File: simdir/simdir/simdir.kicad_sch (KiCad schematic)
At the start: 5 parts, among them U2 MASWSS0178, U3 MASWSS0178, U4 MASWSS0178, U5 MASWSS0178, U6 MASWSS0178

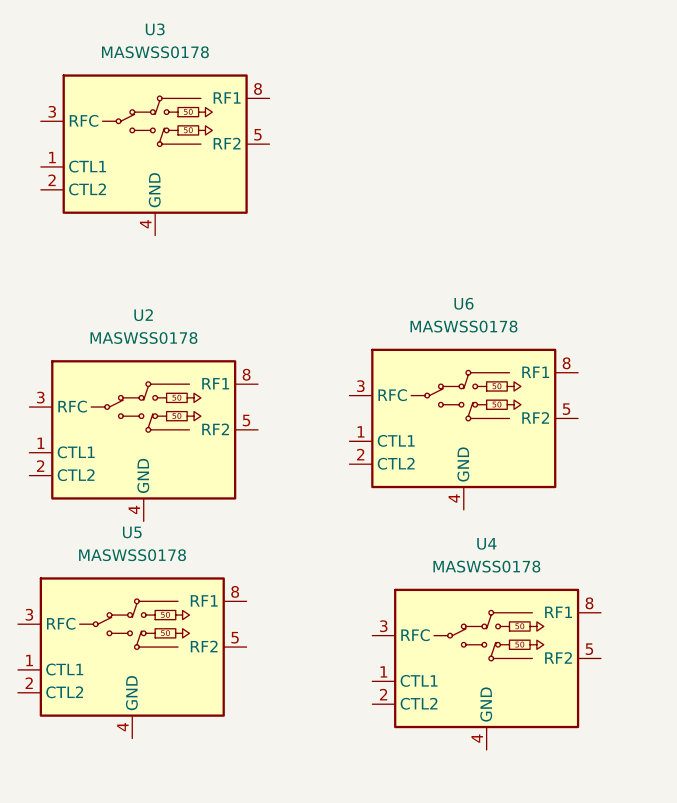
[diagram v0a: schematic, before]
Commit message: Added channel block.
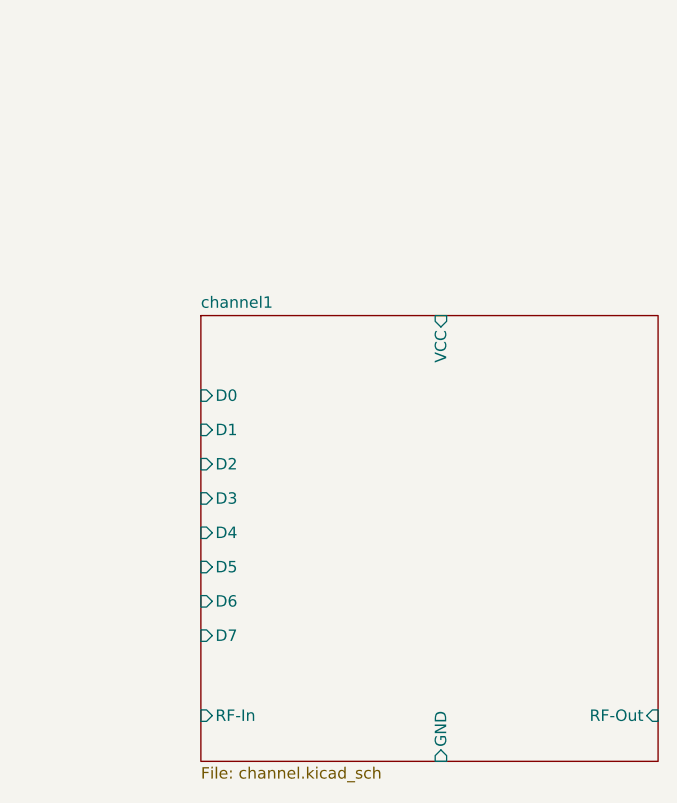
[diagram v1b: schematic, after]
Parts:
- removed U2, U3, U4, U5, U6: MASWSS0178, hand:MSOP-8-1EP_3x3mm_P0.65mm_EP1.73x1.85mm_hand, symbol hand:MASWSS0178
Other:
- added sheet channel1 (channel.kicad_sch)

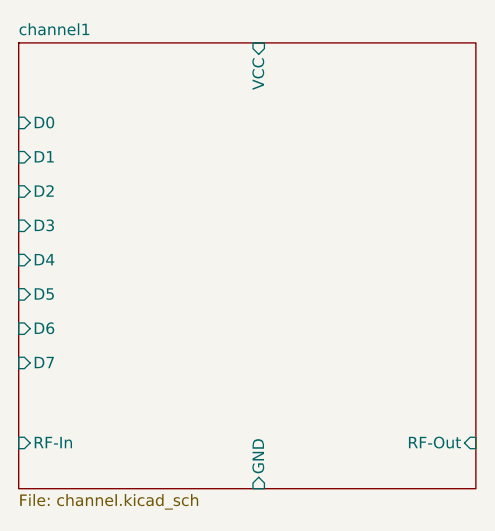
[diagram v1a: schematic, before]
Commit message: Fixed minor issues with channel pins.
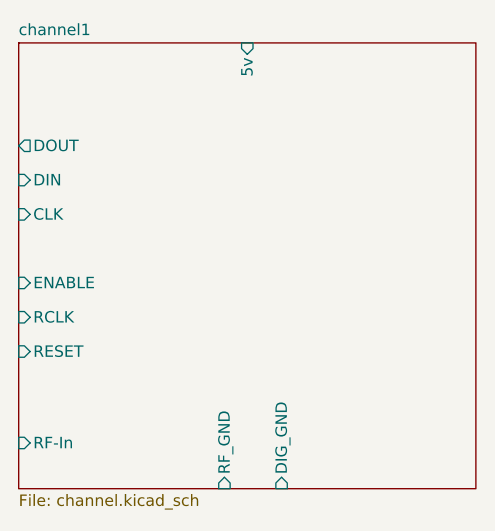
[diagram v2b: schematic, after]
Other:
- sheet channel1 ports: added 5v, CLK, DIG_GND, DIN, DOUT, ENABLE, RCLK, RESET, RF_GND; removed D0, D1, D2, D3, D4, D5, D6, D7, GND, RF-Out, VCC
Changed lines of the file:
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@@
-			)
-		)
-		(pin "D0" input
-			(at 44.45 96.52 180)
-			(effects
-				(font
-					(size 1.27 1.27)
-				)
-				(justify left)
-			)
-		)
-		(pin "D1" input
-			(at 44.45 100.33 180)
-			(effects
-				(font
-					(size 1.27 1.27)
-				)
-				(justify left)
-			)
-		)
-		(pin "D2" input
-			(at 44.45 104.14 180)
-			(effects
-				(font
-					(size 1.27 1.27)
-				)
-				(justify left)
-			)
-		)
-		(pin "D3" input
-			(at 44.45 107.95 180)
-			(effects
-				(font
-					(size 1.27 1.27)
-				)
-				(justify left)
-			)
-		)
-		(pin "D4" input
-			(at 44.45 111.76 180)
-			(effects
-				(font
-					(size 1.27 1.27)
-				)
-				(justify left)
-			)
-		)
-		(pin "D5" input
-			(at 44.45 115.57 180)
-			(effects
-				(font
-					(size 1.27 1.27)
-				)
-				(justify left)
-			)
-		)
-		(pin "D6" input
-			(at 44.45 119.38 180)
-			(effects
-				(font
-					(size 1.27 1.27)
-				)
-				(justify left)
-			)
-		)
-		(pin "D7" input
-			(at 44.45 123.19 180)
-			(effects
-				(font
-					(size 1.27 1.27)
-				)
-				(justify left)
-			)
-		)
-		(pin "GND" input
-			(at 71.12 137.16 270)
-			(effects
-				(font
-					(size 1.27 1.27)
-				)
-				(justify left)
 			)
 		)
@@
 			)
 		)
-		(pin "RF-Out" input
-			(at 95.25 132.08 0)
+		(pin "5v" input
+			(at 69.85 87.63 90)
 			(effects
 				(font
@@
 			)
 		)
-		(pin "VCC" input
-			(at 71.12 87.63 90)
+		(pin "CLK" input
+			(at 44.45 106.68 180)
 			(effects
 				(font
 					(size 1.27 1.27)
 				)
-				(justify right)
+				(justify left)
 			)
 		)
+		(pin "DIG_GND" input
+			(at 73.66 137.16 270)
+			(effects
+				(font
+					(size 1.27 1.27)
+				)
+				(justify left)
+			)
+		)
+		(pin "DIN" input
+			(at 44.45 102.87 180)
+			(effects
+				(font
+					(size 1.27 1.27)
+				)
+				(justify left)
+			)
+		)
+		(pin "DOUT" output
+			(at 44.45 99.06 180)
+			(effects
+				(font
+					(size 1.27 1.27)
+				)
+				(justify left)
+			)
+		)
+		(pin "ENABLE" input
+			(at 44.45 114.3 180)
+			(effects
+				(font
+					(size 1.27 1.27)
+				)
+				(justify left)
+			)
+		)
+		(pin "RCLK" input
+			(at 44.45 118.11 180)
+			(effects
+				(font
+					(size 1.27 1.27)
+				)
+				(justify left)
+			)
+		)
+		(pin "RESET" input
+			(at 44.45 121.92 180)
+			(effects
+				(font
+					(size 1.27 1.27)
+				)
+				(justify left)
+			)
+		)
+		(pin "RF_GND" input
+			(at 67.31 137.16 270)
+			(effects
+				(font
+					(size 1.27 1.27)
+				)
+				(justify left)
+			)
+		)

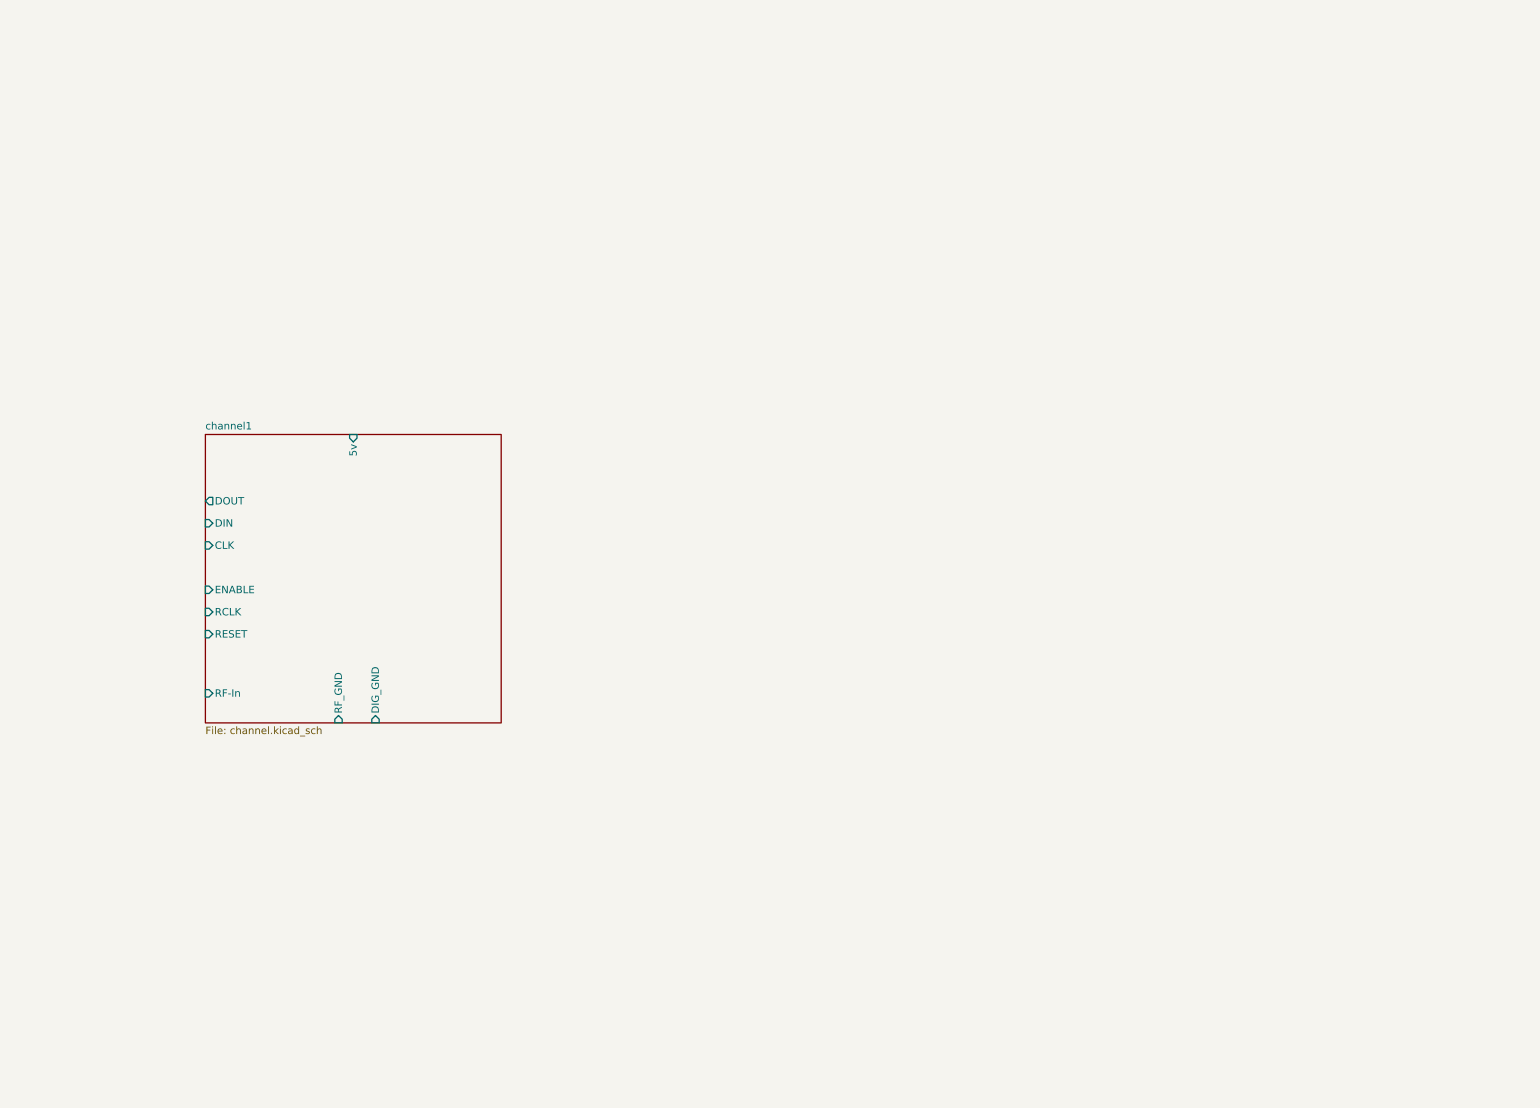
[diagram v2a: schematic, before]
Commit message: Duplicated the channels.
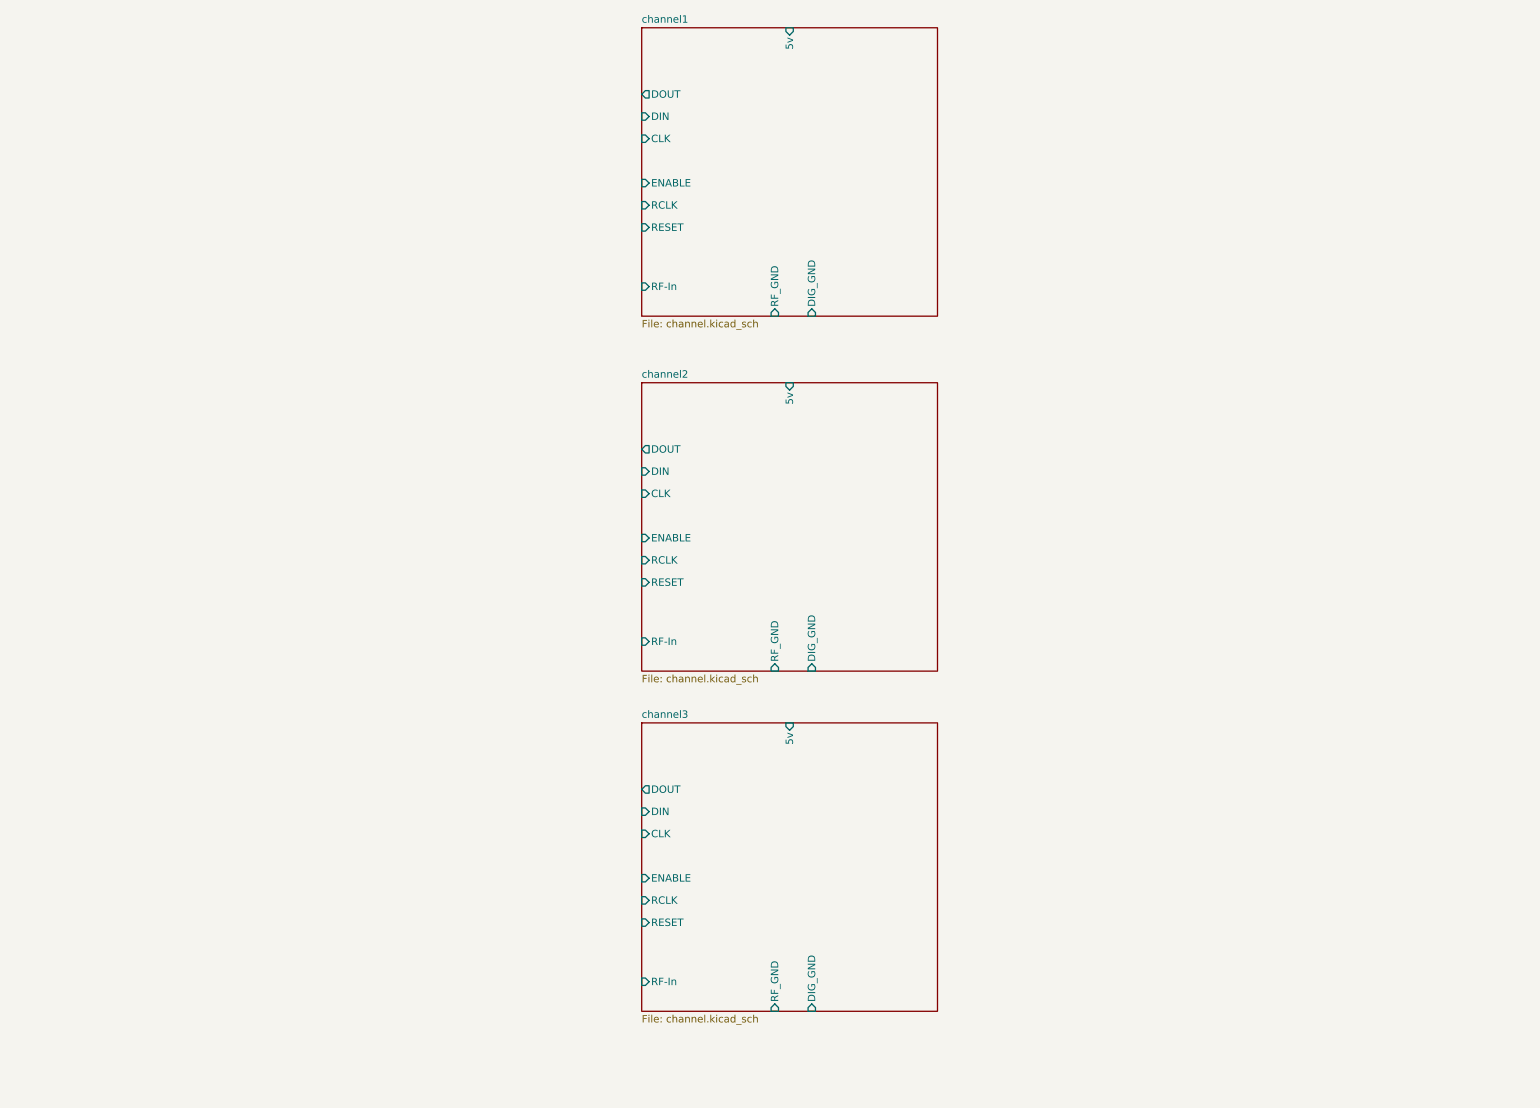
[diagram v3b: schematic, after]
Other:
- added sheet channel2 (channel.kicad_sch)
- added sheet channel3 (channel.kicad_sch)

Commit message: Fixed layout issues & added splitter.
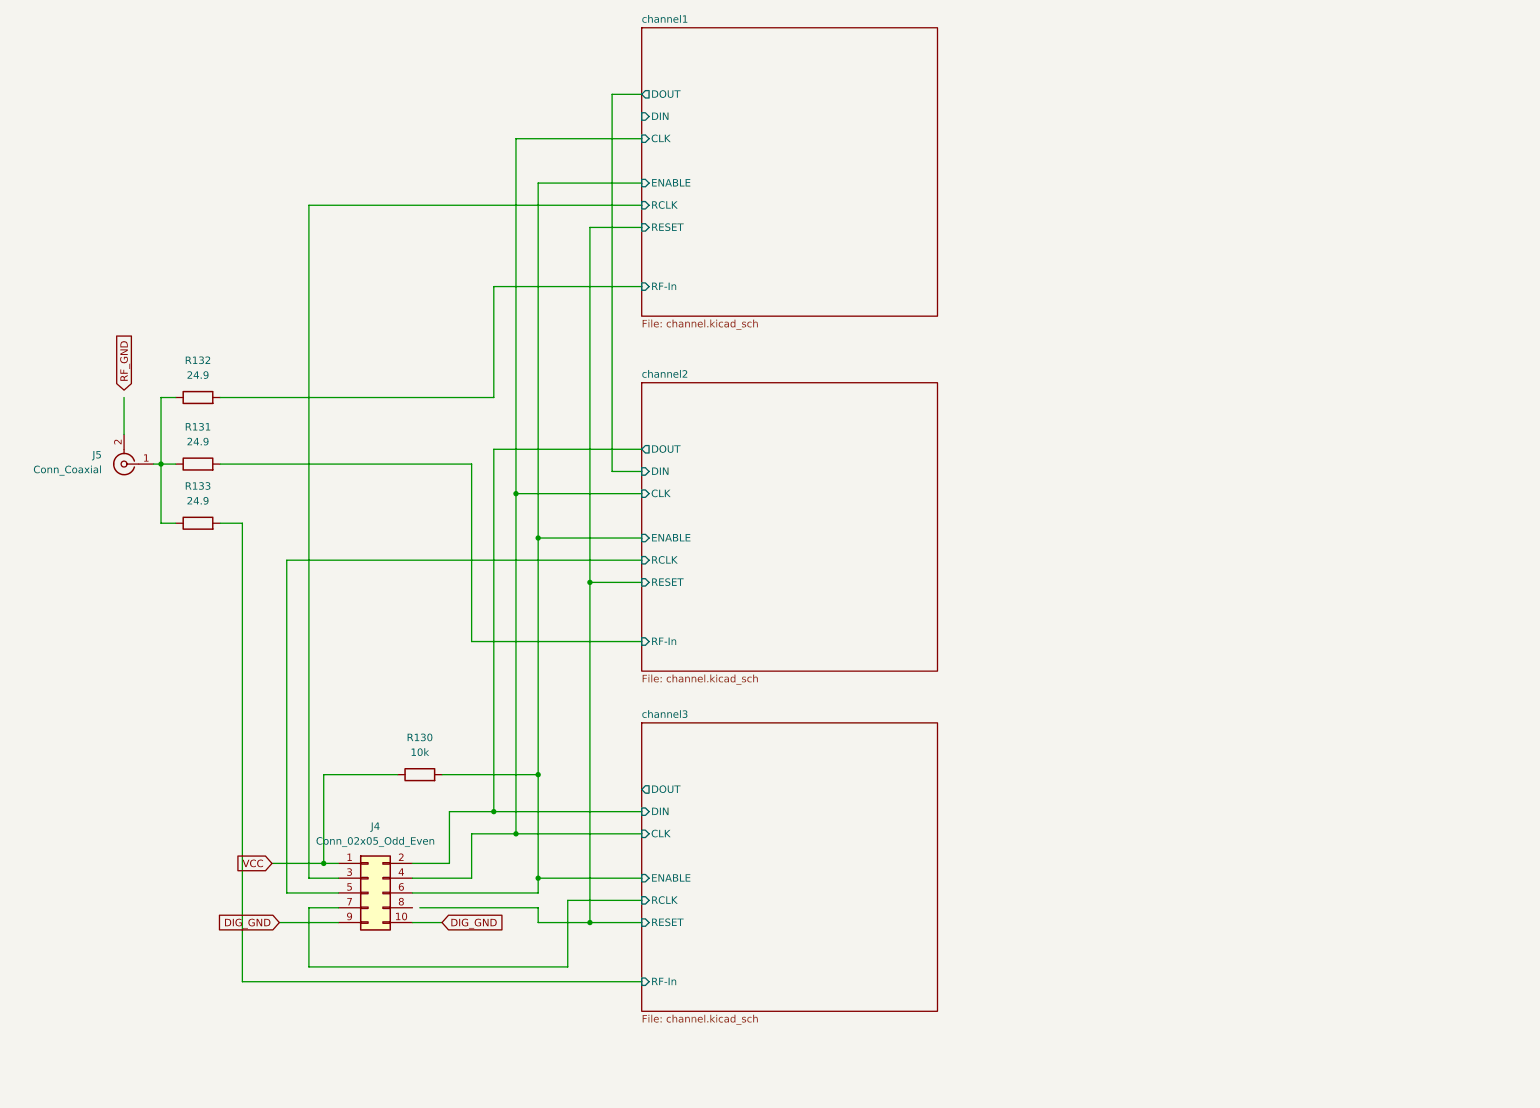
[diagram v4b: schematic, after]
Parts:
- added J4: Conn_02x05_Odd_Even, Connector_PinHeader_2.54mm:PinHeader_2x05_P2.54mm_Vertical, symbol Connector_Generic:Conn_02x05_Odd_Even
- added J5: Conn_Coaxial, Connector_Coaxial:SMA_Amphenol_132289_EdgeMount, symbol Connector:Conn_Coaxial
- added R130: 10k, Resistor_SMD:R_0805_2012Metric_Pad1.20x1.40mm_HandSolder, symbol Device:R
- added R131, R132, R133: 24.9, Resistor_SMD:R_0805_2012Metric_Pad1.20x1.40mm_HandSolder, symbol Device:R
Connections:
- net channel1/CLK: now also J4.4 (Pin_4)
- net channel1/ENABLE: now also J4.6 (Pin_6), R130.2
- net channel1/RCLK: now also J4.3 (Pin_3)
- net channel1/RF-In: now also R132.2
- net channel2/DOUT: now also J4.2 (Pin_2)
- net channel2/RCLK: now also J4.5 (Pin_5)
- net channel2/RF-In: now also R131.2
- net channel3/RCLK: now also J4.7 (Pin_7)
- net channel3/RF-In: now also R133.2
- new net: J5.1 (In), R131.1, R132.1, R133.1
- new net DIG_GND: J4.10 (Pin_10), J4.9 (Pin_9)
- new net VCC: J4.1 (Pin_1), R130.1
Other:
- sheet channel1 ports: added none; removed 5v, DIG_GND, RF_GND
- sheet channel2 ports: added none; removed 5v, DIG_GND, RF_GND
- sheet channel3 ports: added none; removed 5v, DIG_GND, RF_GND

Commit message: Finalized simulation PCB.
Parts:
- added C7: 470n, Capacitor_THT:C_Radial_D10.0mm_H12.5mm_P5.00mm, symbol Device:C
- added C8: 22uF, Capacitor_THT:CP_Radial_D6.3mm_P2.50mm, symbol Device:C_Polarized
- added FB4: FerriteBead, Inductor_SMD:L_0805_2012Metric_Pad1.05x1.20mm_HandSolder, symbol Device:FerriteBead
- added J6: Conn_01x02, Connector_PinHeader_2.54mm:PinHeader_1x02_P2.54mm_Vertical, symbol Connector_Generic:Conn_01x02
- added U58: LM2940CT-5.0, Package_TO_SOT_THT:TO-220-3_Vertical, symbol Regulator_Linear:LM78M05_TO220
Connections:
- net DIG_GND: now also C7.2, C8.2, FB4.2, J6.2 (Pin_2), U58.2 (GND)
- net RF_GND: now also J5.2 (Ext), FB4.1
- net channel1/DIN: now also J4.2 (Pin_2)
- net channel1/RESET: now also J4.8 (Pin_8)
- net channel2/DOUT: no longer J4.2 (Pin_2)
- net VCC renamed 5v
- net 5v: now also C8.1, U58.3 (VO)
- new net: C7.1, J6.1 (Pin_1), U58.1 (VI)

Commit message: Added gerber files.
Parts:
- added R134: 24.9, Resistor_SMD:R_0805_2012Metric_Pad1.20x1.40mm_HandSolder, symbol Device:R
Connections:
- net at R131.1, R132.1, R133.1: now also R134.2; no longer J5.1 (In)
- new net: J5.1 (In), R134.1
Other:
- moved on the sheet: C7, C8, FB4, J4, J6, R130, R131, R132, R133, U58

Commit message: Fixed PCB layout.
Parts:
- removed FB4: FerriteBead, Inductor_SMD:L_0805_2012Metric_Pad1.05x1.20mm_HandSolder, symbol Device:FerriteBead
- added H1, H2, H3, H4: MountingHole_Pad, MountingHole:MountingHole_4.3mm_M4_Pad_Via, symbol Mechanical:MountingHole_Pad
- added NT1: NetTie_2, NetTie:NetTie-2_THT_Pad1.0mm, symbol Device:NetTie_2
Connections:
- net DIG_GND: now also H1.1, H2.1, NT1.1
- net RF_GND: now also H3.1, H4.1, NT1.2

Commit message: Use smaller capacitor and tab-down regulator.
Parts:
- C7: footprint Capacitor_THT:C_Radial_D10.0mm_H12.5mm_P5.00mm -> Capacitor_THT:C_Disc_D4.3mm_W1.9mm_P5.00mm
- U58: footprint Package_TO_SOT_THT:TO-220-3_Vertical -> Package_TO_SOT_THT:TO-220-3_Horizontal_TabDown
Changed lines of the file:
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@@
 			)
 		)
-		(property "Footprint" "Capacitor_THT:C_Radial_D10.0mm_H12.5mm_P5.00mm"
+		(property "Footprint" "Capacitor_THT:C_Disc_D4.3mm_W1.9mm_P5.00mm"
 			(at 210.5152 105.41 0)
 			(hide yes)
@@
 			)
 		)
-		(property "Footprint" "Package_TO_SOT_THT:TO-220-3_Vertical"
+		(property "Footprint" "Package_TO_SOT_THT:TO-220-3_Horizontal_TabDown"
 			(at 222.25 86.995 0)
 			(hide yes)
